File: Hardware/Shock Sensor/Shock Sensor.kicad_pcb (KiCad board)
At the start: 2 copper layers, 7 parts, among them J1 LED, J2 ACCEL, J3 RESET, SW2 ADDRESS, U1 WeMos_mini

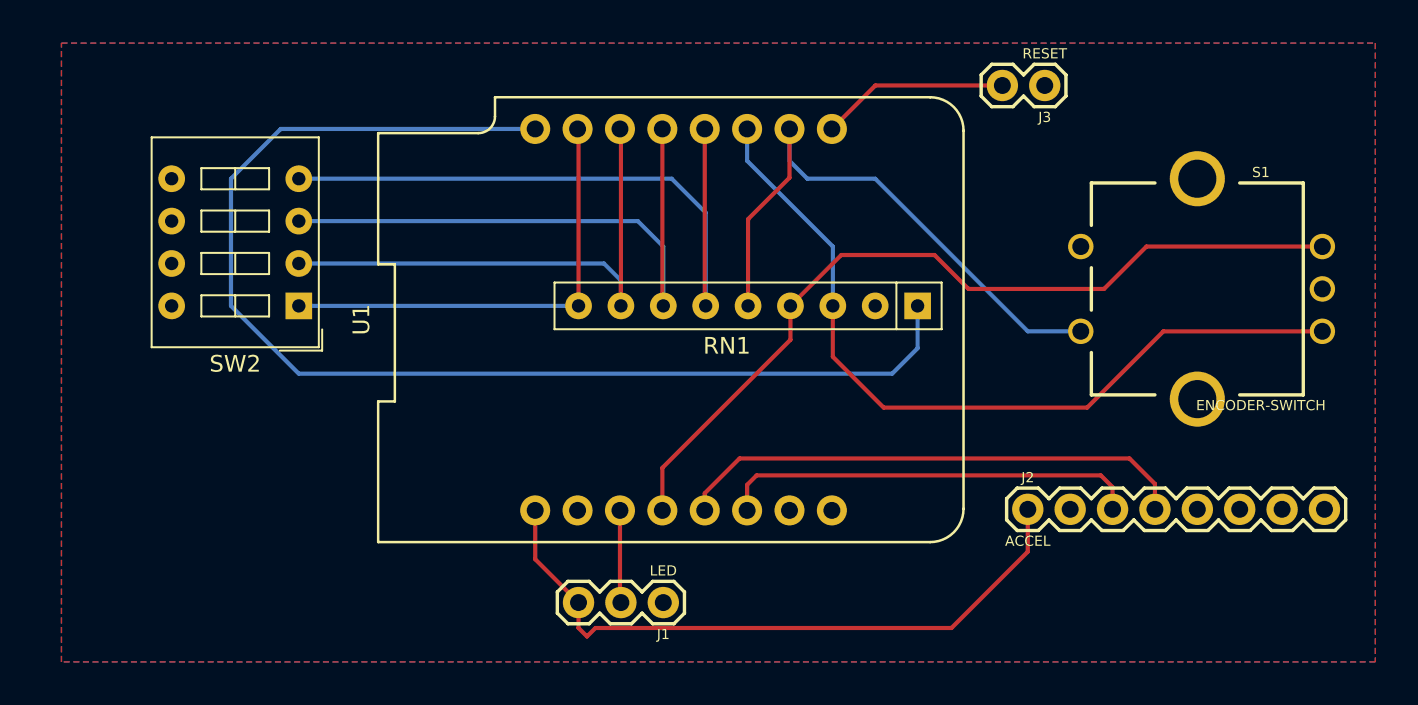
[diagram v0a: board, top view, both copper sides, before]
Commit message: Updates to PCB and code for shock sensors
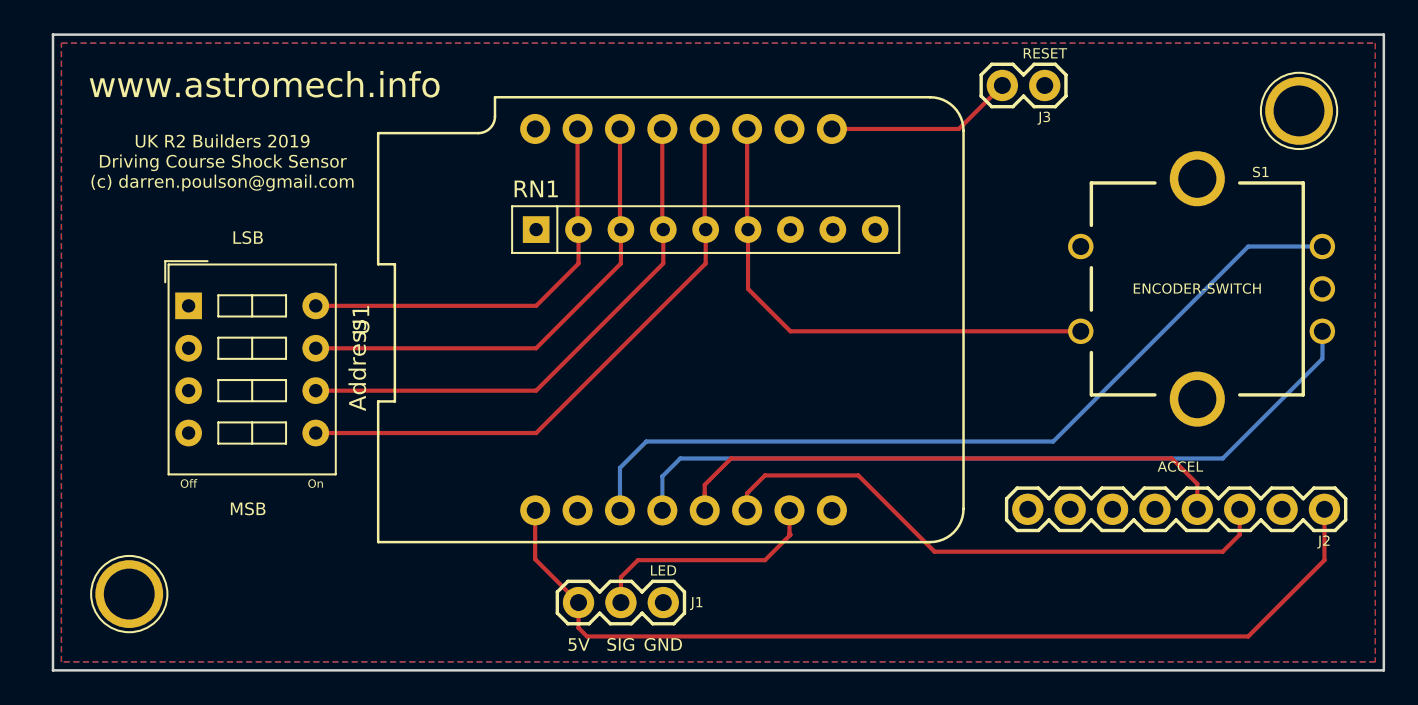
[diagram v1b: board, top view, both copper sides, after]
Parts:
- added REF**: 1pin, Connectors:1pin, F.Cu at (107.7, 127.0)
- added REF**: 1pin, Connectors:1pin, F.Cu at (177.8, 98.0)
- moved RN1 23.3 mm to (132.1, 105.2), turned to 0 degrees
- moved J2 17.8 mm to (179.3, 121.9), turned to 180 degrees
- moved Address 6.60 mm to (111.3, 109.7), turned to 0 degrees
- renumbered SW2 to Address
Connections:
- Address pad 1: Net-(RN1-Pad9) -> GND
- Address pad 2: Net-(RN1-Pad8) -> GND
- Address pad 3: Net-(RN1-Pad7) -> GND
- Address pad 4: Net-(RN1-Pad6) -> GND
- Address pad 5: GND -> Net-(RN1-Pad5)
- Address pad 6: GND -> Net-(RN1-Pad4)
- Address pad 7: GND -> Net-(RN1-Pad3)
- Address pad 8: GND -> Net-(RN1-Pad2)
- S1 pad A: Net-(RN1-Pad3) -> Net-(S1-PadA)
- S1 pad B: Net-(RN1-Pad4) -> Net-(S1-PadB)
- S1 pad SW-: Net-(RN1-Pad5) -> Net-(RN1-Pad6)
- U1 pad 10: Net-(RN1-Pad5) -> Net-(U1-Pad10)
- U1 pad 11: Net-(RN1-Pad3) -> Net-(RN1-Pad6)
- U1 pad 12: Net-(RN1-Pad6) -> Net-(RN1-Pad5)
- U1 pad 13: Net-(RN1-Pad7) -> Net-(RN1-Pad4)
- U1 pad 14: Net-(RN1-Pad8) -> Net-(RN1-Pad3)
- U1 pad 15: Net-(RN1-Pad9) -> Net-(RN1-Pad2)
- U1 pad 3: Net-(J1-Pad2) -> Net-(S1-PadB)
- U1 pad 4: Net-(RN1-Pad4) -> Net-(S1-PadA)
- U1 pad 7: Net-(U1-Pad7) -> Net-(J1-Pad2)
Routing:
- net +3V3: track 73.1 -> 0.00 mm
- net Net-(S1-PadB): track 0.00 -> 50.2 mm
- net Net-(S1-PadA): track 0.00 -> 46.2 mm
- net Net-(RN1-Pad7): track 36.7 -> 0.00 mm
- net Net-(RN1-Pad8): track 31.9 -> 0.00 mm
- net Net-(RN1-Pad9): track 27.4 -> 0.00 mm
- net Net-(RN1-Pad2): track 0.00 -> 25.0 mm
- net Net-(RN1-Pad3): track 48.3 -> 28.6 mm
- net Net-(RN1-Pad4): track 50.5 -> 32.1 mm
- net +5V: track 39.9 -> 58.0 mm
- net Net-(RN1-Pad6): track 41.4 -> 30.6 mm
- net Net-(J2-Pad3): track 25.3 -> 34.8 mm
- net Net-(J1-Pad2): track 5.63 -> 14.3 mm
- net Net-(J2-Pad4): track 31.0 -> 34.9 mm
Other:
- board outline added: 79.8 x 38.1 mm
- board text added: "5V"
- board text added: "GND"
- board text added: "LSB"
- board text added: "MSB"
- board text added: "Off"
- board text added: "On"
- board text added: "SIG"
- board text added: "UK R2 Builders 2019 Driving Course Shock Sensor (c) darren.poulson@gmail.com"
- board text added: "www.astromech.info"
